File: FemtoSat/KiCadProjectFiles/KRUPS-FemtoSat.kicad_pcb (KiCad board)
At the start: 4 copper layers, 29.2 x 71.9 mm, 51 parts, among them J1 XT30U Male Connector, J2 54-00170, J3 USB_C_Receptacle_USB2.0_16P, Q1 IRF7410, Q2 IRF7410, SW1 Enable Switch, SW2 Enclosure Detector, SW3 Enclosure Detector, U1 BME280, U2 ESP32-S3-WROOM-2, U3 TSR_2-2450, U4 TPS61023, U5 E22-900M33S, U6 TPS2117, U7 BNO086, U8 AZ1117-3.3

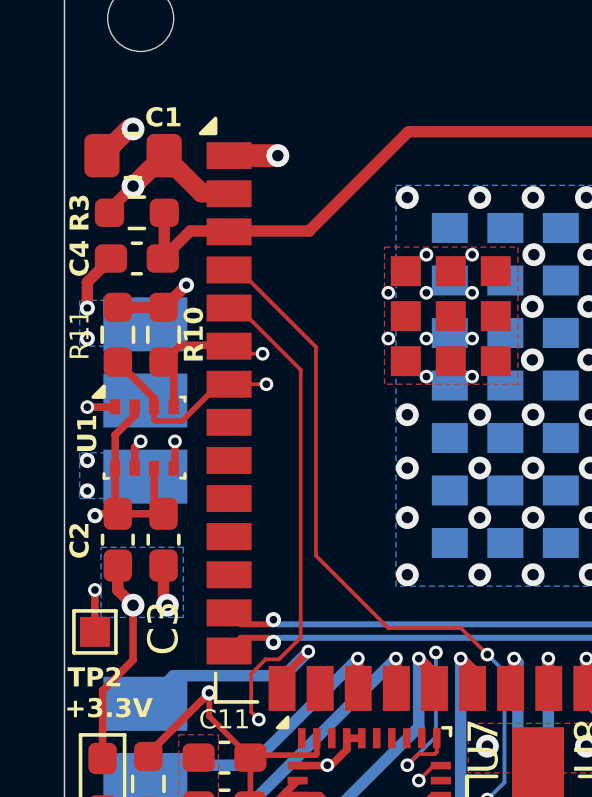
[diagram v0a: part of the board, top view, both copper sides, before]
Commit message: Added optional support for the LR62XE 1W radio
- Created a breakout/adapter board for the LR62XE 1W LoRa radio
- Modified the FemtoSat and RocketStation so that they'll be compatible with the adapter board
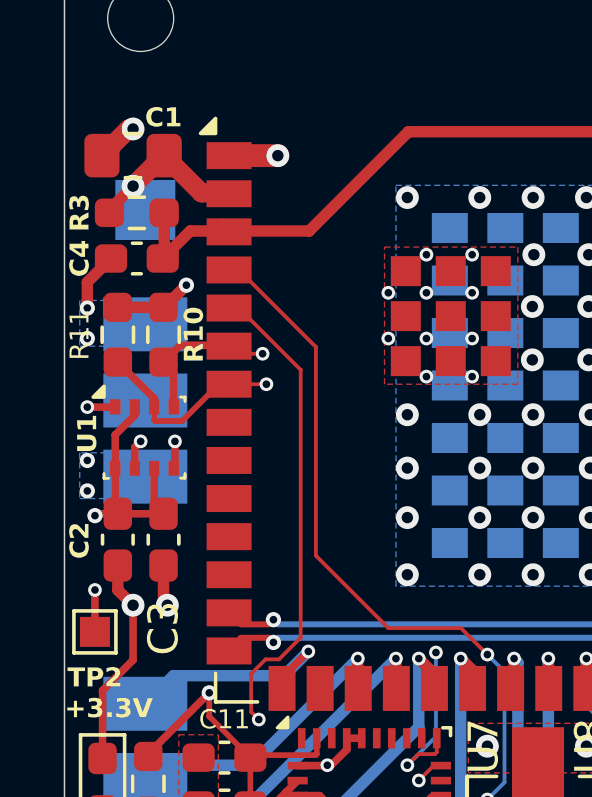
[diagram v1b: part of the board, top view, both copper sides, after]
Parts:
- added TP4: TestPoint, TestPoint:TestPoint_Pad_2.0x2.0mm, B.Cu at (91.6, 31.5)
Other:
- board text added: "UNIVERSITY OF KENTUCKY KRUPS-FEMTOSAT V4 | 12-05-2024 SERIAL NUMBER:"
- board text removed: "UNIVERSITY OF KENTUCKY KRUPS-FEMTOSAT V3 | 11-11-2024 SERIAL NUMBER:"
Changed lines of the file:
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@@
 	(title_block
 		(date "2024-11-11")
-		(rev "V3")
+		(rev "V4")
 	)
 	(layers
@@
 		)
 	)
+	(footprint "TestPoint:TestPoint_Pad_2.0x2.0mm"
+		(layer "B.Cu")
+		(at 91.595 31.53 180)
+		(descr "SMD rectangular pad as test Point, square 2.0mm side length")
+		(tags "test point SMD pad rectangle square")
+		(property "Reference" "TP4"
+			(at 1.933 0.034 -90)
+			(layer "B.SilkS")
+			(effects
+				(font
+					(size 1 1)
+					(thickness 0.15)
+				)
+				(justify mirror)
+			)
+		)
+		(property "Value" "TestPoint"
+			(at 0 -2.05 0)
+			(layer "B.Fab")
+			(effects
+				(font
+					(size 1 1)
+					(thickness 0.15)
+				)
+				(justify mirror)
+			)
+		)
+		(property "Footprint" "TestPoint:TestPoint_Pad_2.0x2.0mm"
+			(at 0 0 0)
+			(unlocked yes)
+			(layer "B.Fab")
+			(hide yes)
+			(effects
+				(font
+					(size 1.27 1.27)
+					(thickness 0.15)
+				)
+				(justify mirror)
+			)
+		)
+		(property "Datasheet" ""
+			(at 0 0 0)
+			(unlocked yes)
+			(layer "B.Fab")
+			(hide yes)
+			(effects
+				(font
+					(size 1.27 1.27)
+					(thickness 0.15)
+				)
+				(justify mirror)
+			)
+		)
+		(property "Description" "test point"
+			(at 0 0 0)
+			(unlocked yes)
+			(layer "B.Fab")
+			(hide yes)
+			(effects
+				(font
+					(size 1.27 1.27)
+					(thickness 0.15)
+				)
+				(justify mirror)
+			)
+		)
+		(property ki_fp_filters "Pin* Test*")
+		(sheetname "Root")
+		(sheetfile "KRUPS-FemtoSat.kicad_sch")
+		(attr exclude_from_pos_files exclude_from_bom)
+		(fp_line
+			(start 1.2 1.2)
+			(end -1.2 1.2)
+			(stroke
+				(width 0.12)
+				(type solid)
+			)
+			(layer "B.SilkS")
+		)
+		(fp_line
+			(start 1.2 -1.2)
+			(end 1.2 1.2)
+			(stroke
+				(width 0.12)
+				(type solid)
+			)
+			(layer "B.SilkS")
+		)
+		(fp_line
+			(start -1.2 1.2)
+			(end -1.2 -1.2)
+			(stroke
+				(width 0.12)
+				(type solid)
+			)
+			(layer "B.SilkS")
+		)
+		(fp_line
+			(start -1.2 -1.2)
+			(end 1.2 -1.2)
+			(stroke
+				(width 0.12)
+				(type solid)
+			)
+			(layer "B.SilkS")
+		)
+		(fp_line
+			(start 1.5 1.5)
+			(end 1.5 -1.5)
+			(stroke
+				(width 0.05)
+				(type solid)
+			)
+			(layer "B.CrtYd")
+		)
+		(fp_line
+			(start 1.5 1.5)
+			(end -1.5 1.5)
+			(stroke
+				(width 0.05)
+				(type solid)
+			)
+			(layer "B.CrtYd")
+		)
+		(fp_line
+			(start -1.5 -1.5)
+			(end 1.5 -1.5)
+			(stroke
+				(width 0.05)
+				(type solid)
+			)
+			(layer "B.CrtYd")
+		)
+		(fp_line
+			(start -1.5 -1.5)
+			(end -1.5 1.5)
+			(stroke
+				(width 0.05)
+				(type solid)
+			)
+			(layer "B.CrtYd")
+		)
+		(fp_text user "${REFERENCE}"
+			(at 0 2 0)
+			(layer "B.Fab")
+			(effects
+				(font
+					(size 1 1)
+					(thickness 0.15)
+				)
+				(justify mirror)
+			)
+		)
+		(pad "1" smd rect
+			(at 0 0 180)
+			(size 2 2)
+			(layers "B.Cu" "B.Mask")
+			(net 5 "+3V3")
+			(pinfunction "1")
+			(pintype "passive")
+		)
+	)
 	(footprint "KRUPS-FemtoSat:E22-XXXM33S"
 		(layer "B.Cu")
@@
 		(sheetname "Root")
 		(sheetfile "KRUPS-FemtoSat.kicad_sch")
+		(attr exclude_from_bom)
 		(fp_line
 			(start 19.65 12.725)
@@
 		(layer "Edge.Cuts")
 	)
-	(gr_text "UNIVERSITY OF KENTUCKY\nKRUPS-FEMTOSAT\nV3 | 11-11-2024\nSERIAL NUMBER:"
+	(gr_text "UNIVERSITY OF KENTUCKY\nKRUPS-FEMTOSAT\nV4 | 12-05-2024\nSERIAL NUMBER:"
 		(at 112.776 28.956 0)
 		(layer "B.SilkS")
@@
 			)
 		)
-	)
-	(zone
-		(net 2)
-		(net_name "GND")
-		(layer "B.Cu")
-		(hatch edge 0.5)
-		(priority 16)
-		(connect_pads thru_hole_only
-			(clearance 0.254)
-		)
-		(min_thickness 0.25)
-		(filled_areas_thickness no)
-		(fill yes
-			(thermal_gap 0.5)
-			(thermal_bridge_width 0.5)
-		)
-		(polygon
-			(pts
-				(xy 90.1192 42.7736) (xy 92.8624 42.7736) (xy 92.8624 45.1104) (xy 90.1192 45.1104)
-			)
-		)

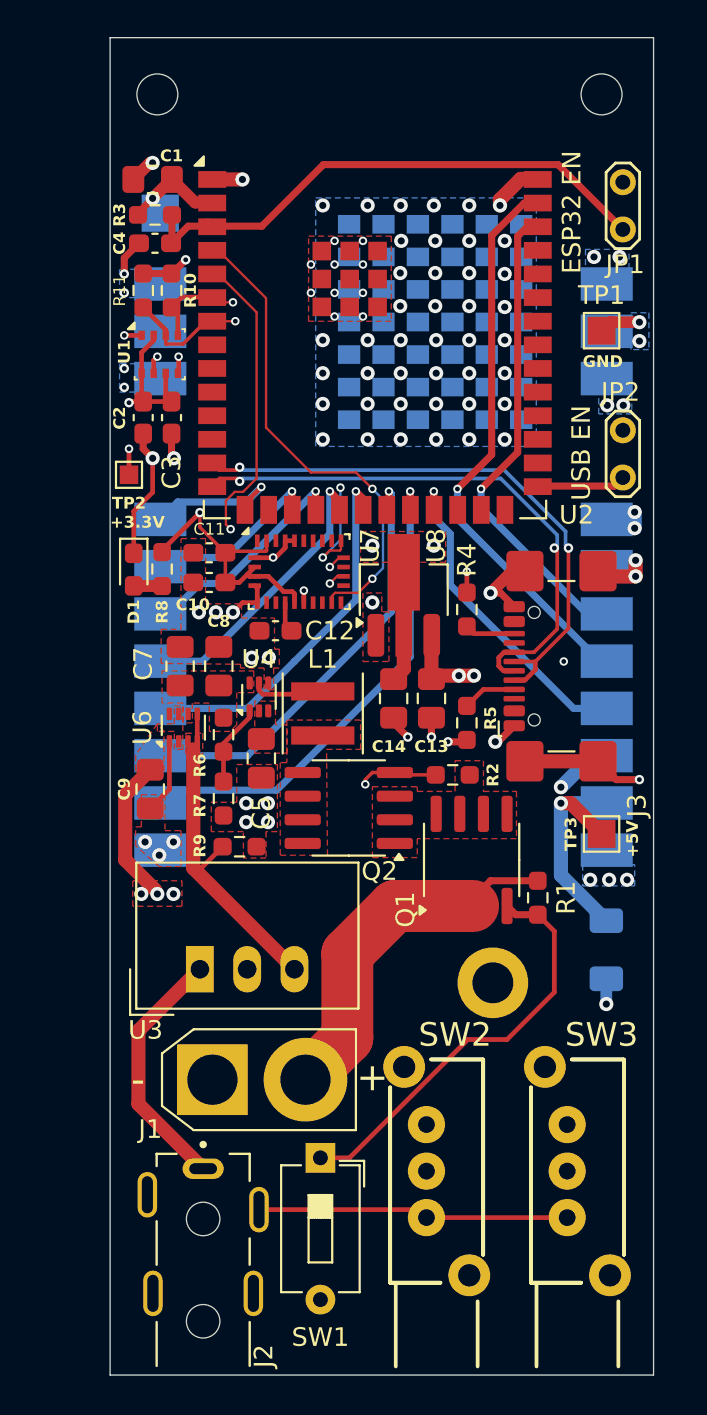
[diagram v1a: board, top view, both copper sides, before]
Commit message: Design Review Updates
Large number of design changes to both the FemtoSat (V5) and RocketStation (V3)

On both boards:
- Swapped the ESP32-S3-WROOM-2 modules to WROOM-1 modules due to supply issues
- Swapped power connectors to JST VH, data connectors to JST GH
- Added "Space Systems Lab, University of Kentucky, Lexington KY, USA, Earth" to the silkscreens
- Added test pads for IO pins, I2C bus, power
- Added LEDs connected to IO pins
- Changed power indication LEDs to a brighter LED
- Reformatted BOMs, they can now be generated by KiCad rather than being made by hand
- Updated documentation, 3D models

For Femtosat
- Removed 1 enclosure switch & MOSFET
- Moved a screw hole

and a bunch of other minor changes that I've forgotten
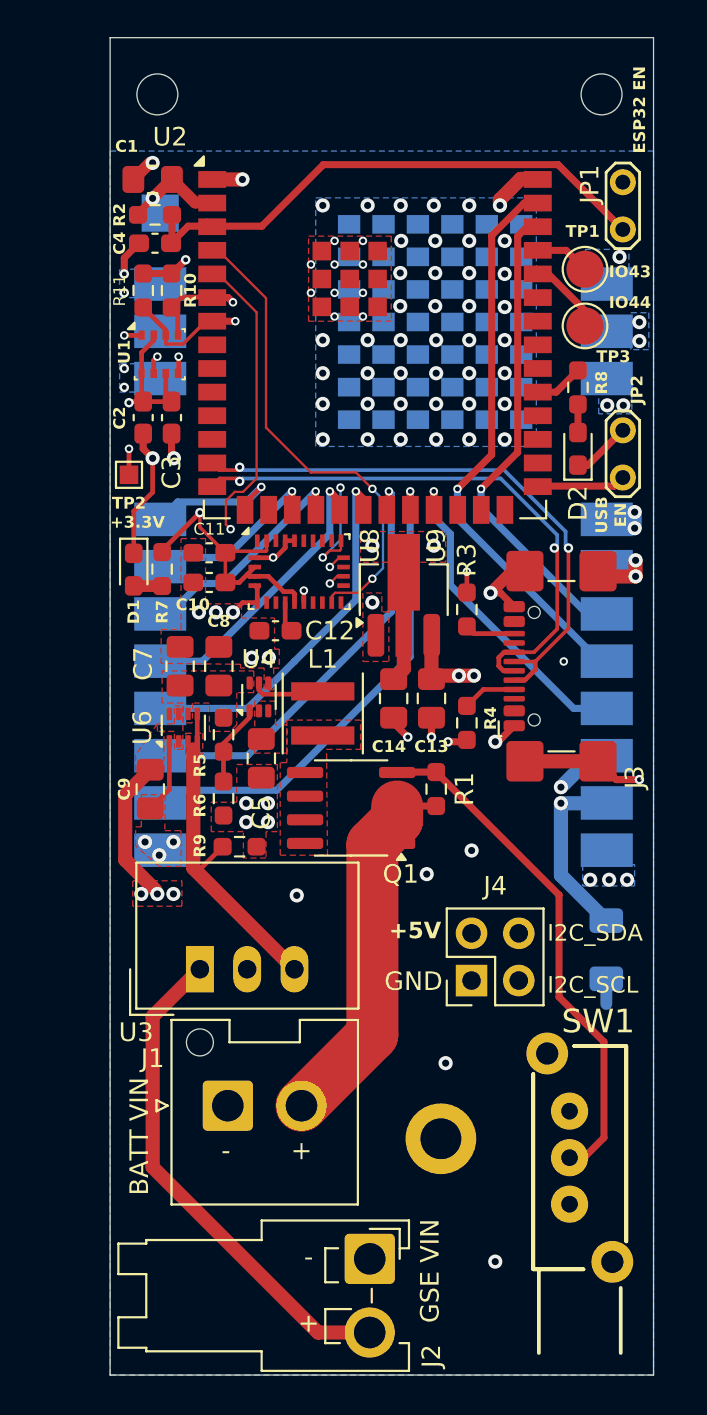
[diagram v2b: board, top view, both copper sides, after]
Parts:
- removed Q2: IRF7410, Package_SO:SOIC-8_3.9x4.9mm_P1.27mm
- removed the R2 at (107.3, 61.7)
- removed the SW1 at (100.2, 82.3)
- removed SW3: Enclosure Detector, KRUPS-FemtoSat:LC1258OANP
- added D2: LED, Diode_SMD:D_0603_1608Metric_Pad1.05x0.95mm_HandSolder, F.Cu at (114.0, 44.2)
- added J4: Conn_02x02, Connector_PinHeader_2.54mm:PinHeader_2x02_P2.54mm_Vertical, F.Cu at (108.3, 72.8)
- added R8: 68, Resistor_SMD:R_0603_1608Metric_Pad0.98x0.95mm_HandSolder, F.Cu at (114.0, 40.9)
- J1: value XT30U Male Connector -> B2P-VH-FB-B; footprint Connector_AMASS:AMASS_XT30U-M_1x02_P5.0mm_Vertical -> Connector_JST:JST_VH_B2P-VH-FB-B_1x02_P3.96mm_Vertical
- J2: value 54-00170 -> B2PS-VH; footprint KRUPS-FemtoSat:TENSILITY_54-00170 -> Connector_JST:JST_VH_S2P-VH_1x02_P3.96mm_Horizontal
- R7: renamed from R8; value 270 -> 68
- TP1: value GND -> TestPoint; footprint TestPoint:TestPoint_Pad_1.5x1.5mm -> TestPoint:TestPoint_Pad_D2.0mm
- TP3: value +5V -> TestPoint; footprint TestPoint:TestPoint_Pad_1.5x1.5mm -> TestPoint:TestPoint_Pad_D2.0mm
- moved TP3 27.3 mm to (114.4, 37.6), turned to 0 degrees
- moved J2 8.97 mm to (102.9, 87.7), turned to -90 degrees
- moved H3 8.84 mm to (106.7, 81.3)
- moved R1 8.00 mm to (106.4, 62.5), turned to 90 degrees
- moved SW1 7.72 mm to (113.6, 79.8)
- moved Q1 7.05 mm to (101.9, 63.5), turned to 180 degrees
- moved TP1 3.42 mm to (114.4, 34.5)
- moved J1 1.62 mm to (95.2, 79.5)
- renumbered R3 to R2, R4 to R3, R5 to R4, R6 to R5, R7 to R6, SW2 to SW1, U7 to U8, U8 to U9
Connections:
- J2 pad 1: /GSE_VIN -> GND
- J2 pad 2: GND -> /GSE_VIN
- Q1 pad 5: Net-(Q1-D) -> /BATT_VIN
- Q1 pad 6: Net-(Q1-D) -> /BATT_VIN
- Q1 pad 7: Net-(Q1-D) -> /BATT_VIN
- Q1 pad 8: Net-(Q1-D) -> /BATT_VIN
- SW1 pad 1: /PLUG_SWITCH -> GND
- SW1 pad 2: Net-(SW1-B) -> Net-(Q1-G)
- TP1 pad 1: GND -> /IO43
- TP3 pad 1: +5V -> /IO44
- U2 pad 31: unconnected-(U2-IO38-Pad31) -> /GPIO_LED
- U2 pad 36: unconnected-(U2-RXD0/IO44-Pad36) -> /IO44
- U2 pad 37: unconnected-(U2-TXD0/IO43-Pad37) -> /IO43
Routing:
- net /I2C_SCL: track 31.4 -> 62.9 mm
- net /I2C_SDA: track 23.8 -> 53.7 mm
- net Net-(Q2-G): track 29.6 -> 0.00 mm, vias 1 -> 0
- net /PLUG_SWITCH: track 16.7 -> 0.00 mm
- net /GSE_VIN: track 13.5 -> 27.0 mm
- net Net-(SW1-B): track 9.27 -> 0.00 mm
- net +5V: track 59.3 -> 67.8 mm
- net Net-(Q1-G): track 22.7 -> 28.1 mm
- net /IO44: track 0.00 -> 4.18 mm
- net /IO43: track 0.00 -> 2.96 mm
- net /GPIO_LED: track 0.00 -> 2.64 mm
- net Net-(D2-A): track 0.00 -> 1.51 mm
- net GND: track 61.5 -> 62.4 mm, vias 100 -> 103
- net Net-(J1-Pin_2): track 19.6 -> 20.3 mm
- removed copper zone on F.Cu, net Net-(Q1-D)
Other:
- board text added: "+"
- board text added: "-"
- board text added: "3.0V TO 4.35V"
- board text added: "6.5V TO 36V"
- board text added: "BATT VIN"
- board text added: "GSE VIN"
- board text added: "I2C_SCL"
- board text added: "I2C_SDA"
- board text added: "IO43"
- board text added: "IO44"
- board text added: "JST-VH"
- board text added: "KRUPS-FEMTOSAT V5 | 12-27-2024 SERIAL NUMBER:"
- board text added: "Space Systems Lab University of Kentucky Lexington KY, USA, Earth"
- board text removed: "UNIVERSITY OF KENTUCKY KRUPS-FEMTOSAT V4 | 12-05-2024 SERIAL NUMBER:"

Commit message: Added fiducials to femtosat (v6) and rocketstation (v4)
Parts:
- added FID1: Fiducial, Fiducial:Fiducial_0.5mm_Mask1mm, F.Cu at (108.5, 91.9)
- added FID2: Fiducial, Fiducial:Fiducial_0.5mm_Mask1mm, F.Cu at (114.0, 31.2)
- added FID3: Fiducial, Fiducial:Fiducial_0.5mm_Mask1mm, F.Cu at (101.1, 55.1)
- U2: value ESP32-S3-WROOM-2 -> ESP32-S3-WROOM-1-N16R8
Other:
- board text added: "KRUPS-FEMTOSAT V6 | 12-28-2024 SERIAL NUMBER:"
- board text removed: "KRUPS-FEMTOSAT V5 | 12-27-2024 SERIAL NUMBER:"
